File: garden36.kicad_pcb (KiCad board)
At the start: 2 copper layers, 112.1 x 90.7 mm, 41 parts, among them J1 Conn_01x02, SW1 SW_SPDT, SW2 SW_Push, U1 nice_nano

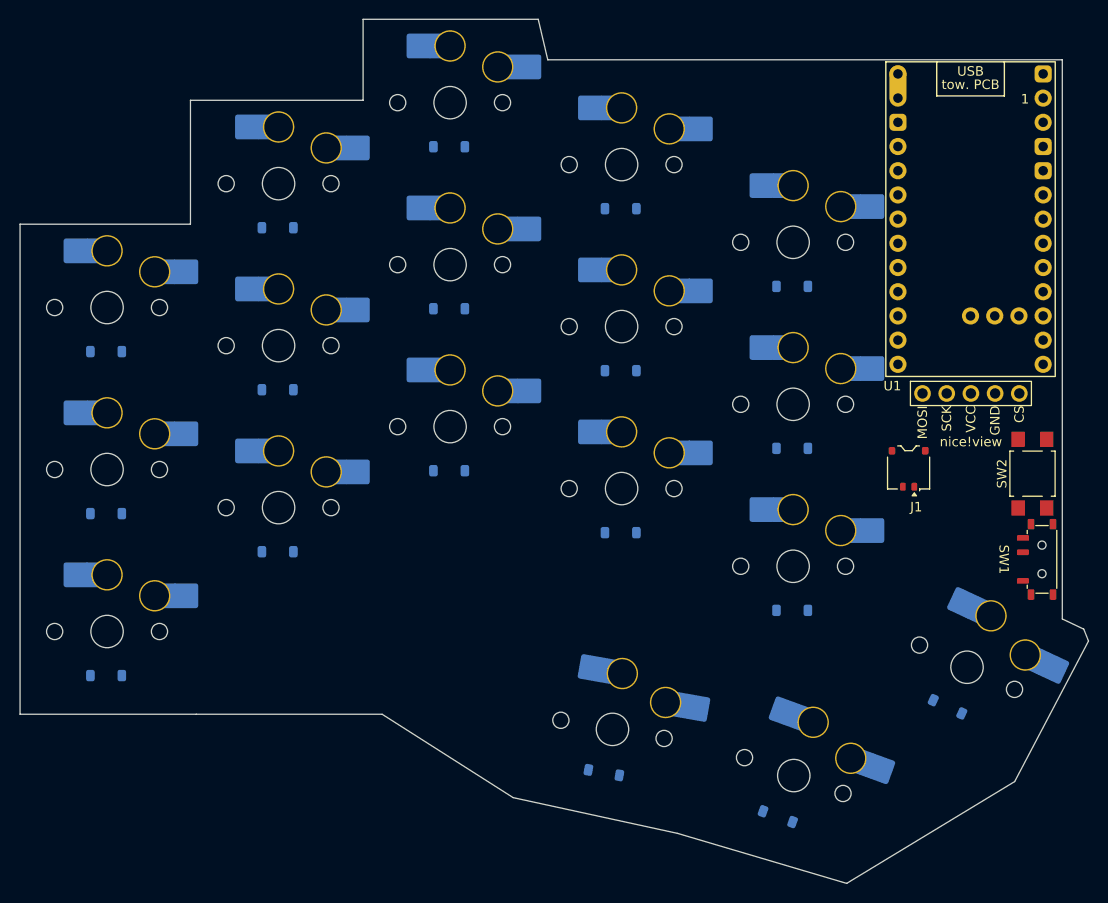
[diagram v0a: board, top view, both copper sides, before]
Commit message: Finished trace routing for left part
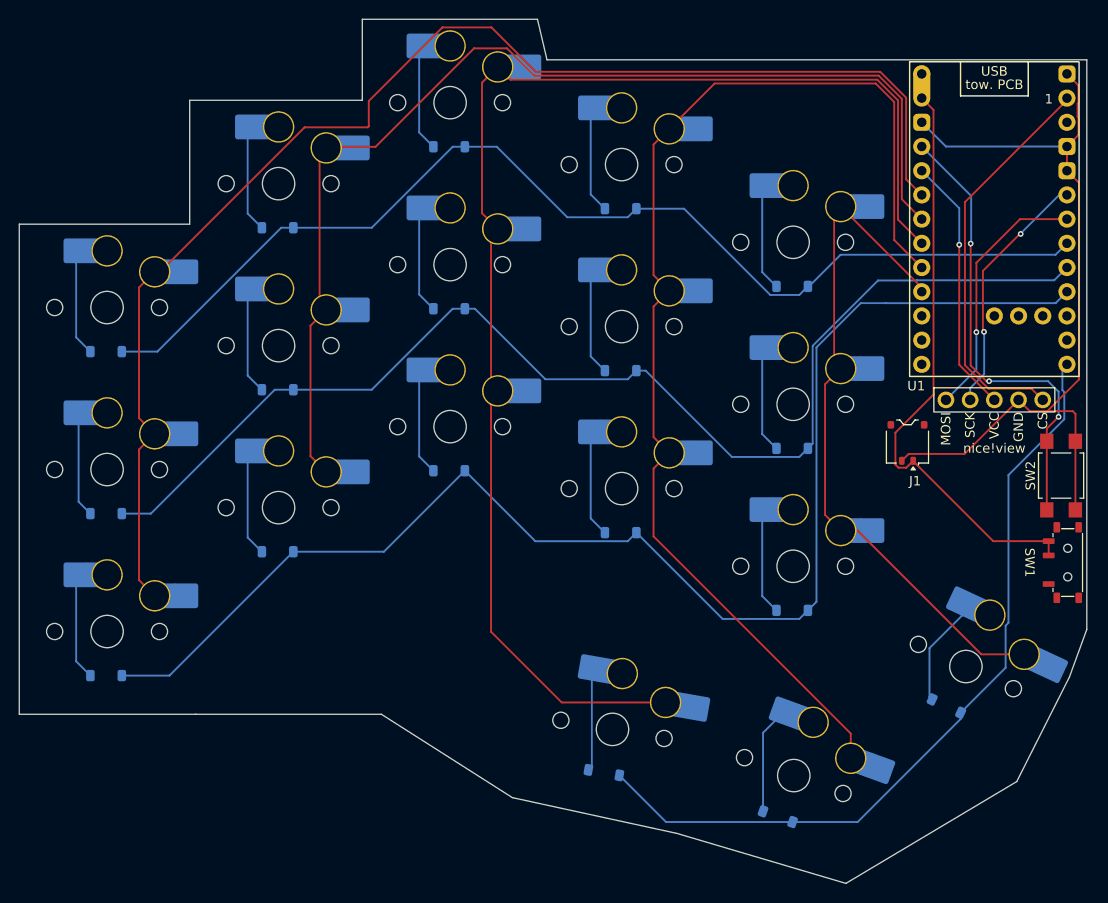
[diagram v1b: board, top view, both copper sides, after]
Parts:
- moved SW2 3.01 mm to (140.4, 96.6)
- moved J1 2.73 mm to (124.3, 93.2)
- moved SW1 2.72 mm to (141.1, 105.8)
- moved Display1 2.55 mm to (133.4, 72.2)
- moved U1 2.50 mm to (133.4, 71.0)
- moved CH18 0.14 mm to (130.4, 116.7)
- moved D18 0.14 mm to (128.4, 120.8)
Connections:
- U1 pad 10: ROW3 -> unconnected-(U1-P0.11-Pad10)
- U1 pad 12: unconnected-(U1-P1.06-LF-Pad12) -> ROW3
- U1 pad 17: unconnected-(U1-P0.31-LF-Pad17) -> COL0
- U1 pad 18: COL0 -> COL1
- U1 pad 19: COL1 -> COL2
- U1 pad 20: COL2 -> COL3
- U1 pad 21: COL3 -> COL4
- U1 pad 22: COL4 -> unconnected-(U1-P1.11-LF-Pad22)
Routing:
- net ROW2: track 0.00 -> 145.1 mm
- net COL2: track 0.00 -> 144.1 mm
- net COL0: track 0.00 -> 142.3 mm
- net ROW1: track 0.00 -> 129.5 mm
- net COL3: track 0.00 -> 123.7 mm
- net ROW0: track 0.00 -> 117.5 mm
- net COL1: track 0.00 -> 117.4 mm
- net GND: track 0.00 -> 86.2 mm
- net ROW3: track 0.00 -> 84.3 mm
- net COL4: track 0.00 -> 73.0 mm
- net BAT: track 0.00 -> 62.2 mm
- net RST: track 0.00 -> 48.4 mm, vias 0 -> 3
- net CS: track 0.00 -> 42.3 mm
- net +3.3V: track 0.00 -> 27.2 mm, vias 0 -> 1
- net MOSI: track 0.00 -> 27.1 mm, vias 0 -> 1
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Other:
- board size 112.1 x 90.7 mm -> 112 x 90.7 mm

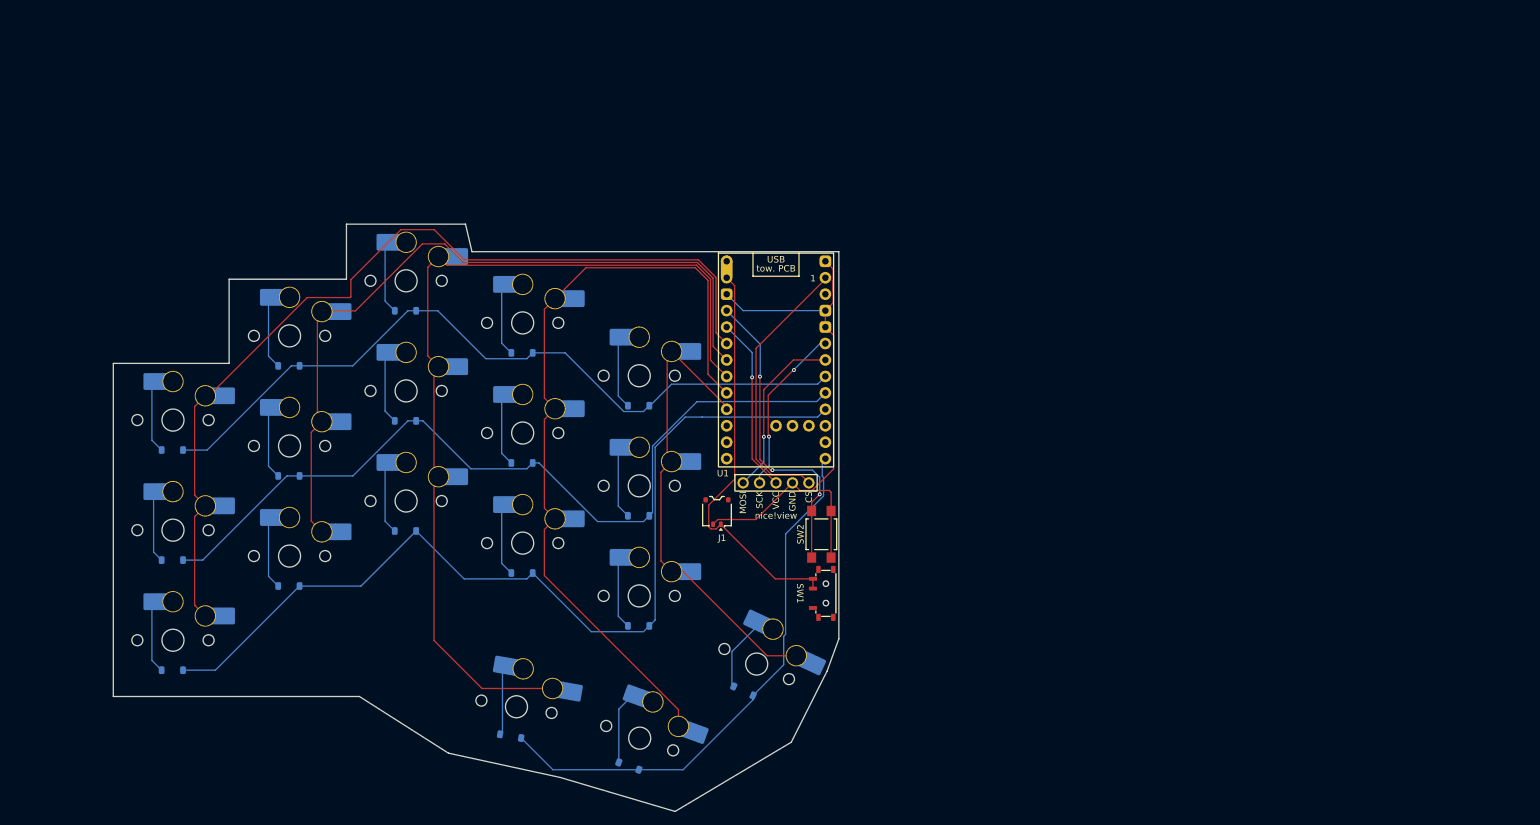
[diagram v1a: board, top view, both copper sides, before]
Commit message: Add right half of keyboard
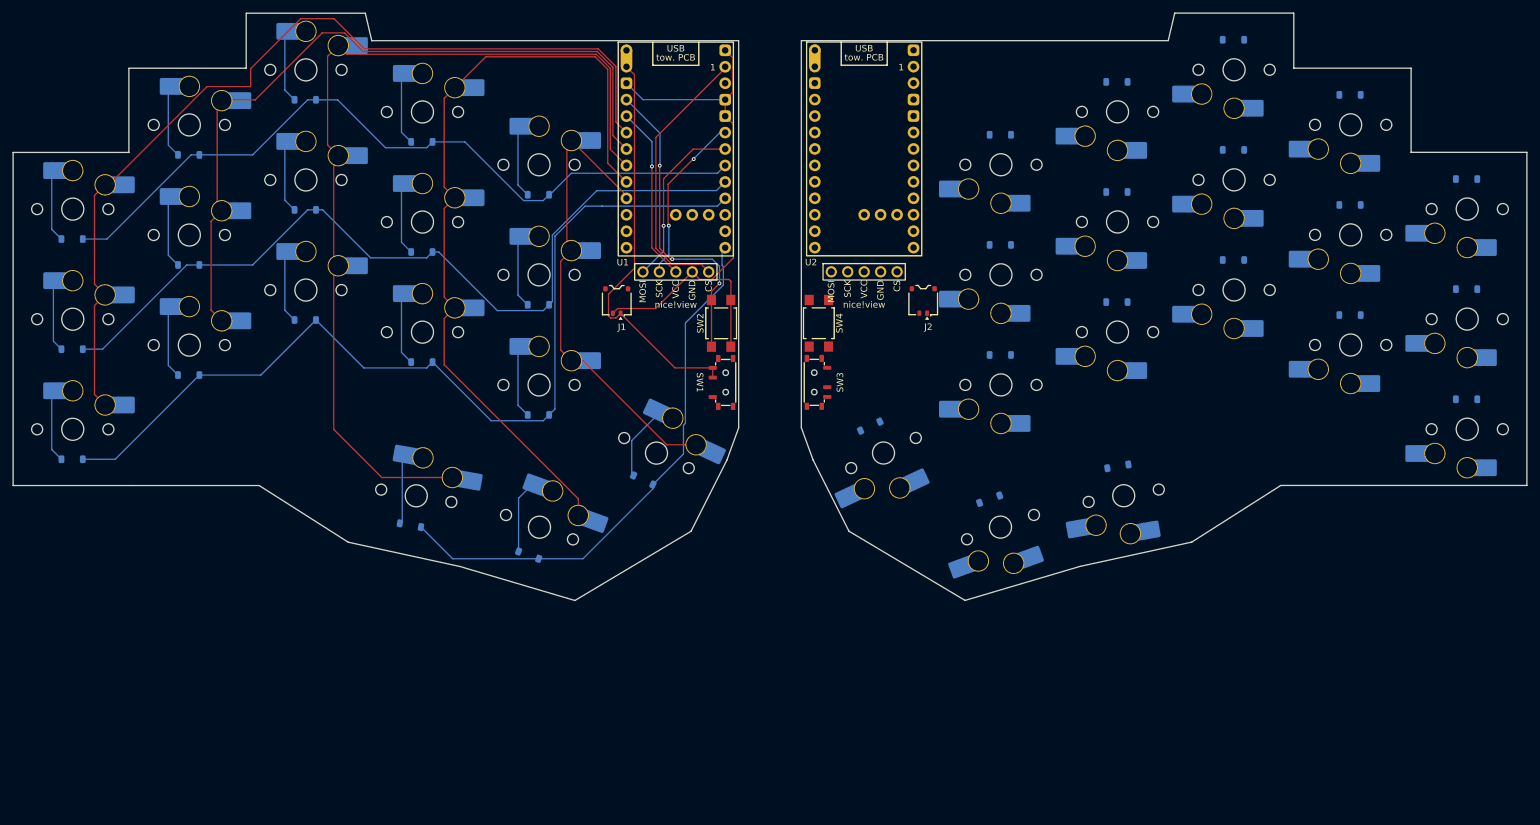
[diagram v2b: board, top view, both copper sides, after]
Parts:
- added CH19: choc_v1_SW_HS, PCM_marbastlib-choc:SW_choc_v1_HS_CPG135001S30_1u, B.Cu at (240.1, 46.4)
- added CH20: choc_v1_SW_HS, PCM_marbastlib-choc:SW_choc_v1_HS_CPG135001S30_1u, B.Cu at (222.1, 33.4)
- added CH21: choc_v1_SW_HS, PCM_marbastlib-choc:SW_choc_v1_HS_CPG135001S30_1u, B.Cu at (204.1, 24.9)
- added CH22: choc_v1_SW_HS, PCM_marbastlib-choc:SW_choc_v1_HS_CPG135001S30_1u, B.Cu at (186.1, 31.4)
- added CH23: choc_v1_SW_HS, PCM_marbastlib-choc:SW_choc_v1_HS_CPG135001S30_1u, B.Cu at (168.1, 39.6)
- added CH24: choc_v1_SW_HS, PCM_marbastlib-choc:SW_choc_v1_HS_CPG135001S30_1u, B.Cu at (240.1, 63.4)
- added CH25: choc_v1_SW_HS, PCM_marbastlib-choc:SW_choc_v1_HS_CPG135001S30_1u, B.Cu at (222.1, 50.4)
- added CH26: choc_v1_SW_HS, PCM_marbastlib-choc:SW_choc_v1_HS_CPG135001S30_1u, B.Cu at (204.1, 41.9)
- added CH27: choc_v1_SW_HS, PCM_marbastlib-choc:SW_choc_v1_HS_CPG135001S30_1u, B.Cu at (186.1, 48.4)
- added CH28: choc_v1_SW_HS, PCM_marbastlib-choc:SW_choc_v1_HS_CPG135001S30_1u, B.Cu at (168.1, 56.6)
- added CH29: choc_v1_SW_HS, PCM_marbastlib-choc:SW_choc_v1_HS_CPG135001S30_1u, B.Cu at (240.1, 80.4)
- added CH30: choc_v1_SW_HS, PCM_marbastlib-choc:SW_choc_v1_HS_CPG135001S30_1u, B.Cu at (222.1, 67.4)
- added CH31: choc_v1_SW_HS, PCM_marbastlib-choc:SW_choc_v1_HS_CPG135001S30_1u, B.Cu at (204.1, 58.9)
- added CH32: choc_v1_SW_HS, PCM_marbastlib-choc:SW_choc_v1_HS_CPG135001S30_1u, B.Cu at (186.1, 65.4)
- added CH33: choc_v1_SW_HS, PCM_marbastlib-choc:SW_choc_v1_HS_CPG135001S30_1u, B.Cu at (168.1, 73.6)
- added CH34: choc_v1_SW_HS, PCM_marbastlib-choc:SW_choc_v1_HS_CPG135001S30_1u, B.Cu at (187.1, 90.7)
- added CH35: choc_v1_SW_HS, PCM_marbastlib-choc:SW_choc_v1_HS_CPG135001S30_1u, B.Cu at (168.0, 95.5)
- added CH36: choc_v1_SW_HS, PCM_marbastlib-choc:SW_choc_v1_HS_CPG135001S30_1u, B.Cu at (150.0, 84.1)
- added D19: 1N4148W, Diode_SMD:D_SOD-123, B.Cu at (240.0, 41.8)
- added D20: 1N4148W, Diode_SMD:D_SOD-123, B.Cu at (222.0, 28.8)
- added D21: 1N4148W, Diode_SMD:D_SOD-123, B.Cu at (204.0, 20.3)
- added D22: 1N4148W, Diode_SMD:D_SOD-123, B.Cu at (186.0, 26.8)
- added D23: 1N4148W, Diode_SMD:D_SOD-123, B.Cu at (168.0, 34.9)
- added D24: 1N4148W, Diode_SMD:D_SOD-123, B.Cu at (240.0, 58.8)
- added D25: 1N4148W, Diode_SMD:D_SOD-123, B.Cu at (222.0, 45.8)
- added D26: 1N4148W, Diode_SMD:D_SOD-123, B.Cu at (204.0, 37.3)
- added D27: 1N4148W, Diode_SMD:D_SOD-123, B.Cu at (186.0, 43.8)
- added D28: 1N4148W, Diode_SMD:D_SOD-123, B.Cu at (168.0, 51.9)
- added D29: 1N4148W, Diode_SMD:D_SOD-123, B.Cu at (240.0, 75.8)
- added D30: 1N4148W, Diode_SMD:D_SOD-123, B.Cu at (222.0, 62.8)
- added D31: 1N4148W, Diode_SMD:D_SOD-123, B.Cu at (204.0, 54.3)
- added D32: 1N4148W, Diode_SMD:D_SOD-123, B.Cu at (186.0, 60.8)
- added D33: 1N4148W, Diode_SMD:D_SOD-123, B.Cu at (168.0, 68.9)
- added D34: 1N4148W, Diode_SMD:D_SOD-123, B.Cu at (186.2, 86.1)
- added D35: 1N4148W, Diode_SMD:D_SOD-123, B.Cu at (166.4, 91.2)
- added D36: 1N4148W, Diode_SMD:D_SOD-123, B.Cu at (147.9, 79.9)
- added Display2: nice!view, nice_view:nice_view, F.Cu at (147.0, 39.6)
- added J2: Conn_01x02, PCM_marbastlib-various:CON_JST_ACH_BM02B, F.Cu at (156.1, 60.6)
- added SW3: SW_SPDT, PCM_marbastlib-various:SW_MSK12C02-HB, F.Cu at (139.3, 73.2)
- added SW4: SW_Push, Button_Switch_SMD:SW_SPST_TL3305A, F.Cu at (140.0, 64.0)
- added U2: nice_nano, PCM_marbastlib-xp-promicroish:nice_nano_AH_USBdn, F.Cu at (147.0, 38.4)
- moved CH10 36.1 mm to (96.8, 56.6)
- moved CH13 36.1 mm to (60.8, 58.9)
- moved CH5 36.1 mm to (96.8, 39.6)
- moved CH8 36.1 mm to (60.8, 41.9)
- moved CH9 36.1 mm to (78.8, 48.4)
- moved D1 36.1 mm to (24.7, 51.0)
- moved D10 36.1 mm to (96.7, 61.2)
- moved D2 36.1 mm to (42.7, 38.0)
- moved D4 36.1 mm to (78.7, 36.0)
- moved D5 36.1 mm to (96.7, 44.2)
- moved D7 36.1 mm to (42.7, 55.0)
- moved D9 36.1 mm to (78.7, 53.0)
- moved J1 36.1 mm to (108.8, 60.6)
- moved U1 36.1 mm to (117.9, 38.4)
- moved CH1 36.1 mm to (24.8, 46.4)
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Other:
- board size 112 x 90.7 mm -> 233.7 x 90.7 mm

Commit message: Finished routing for both halfs
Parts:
- moved CH29 72.9 mm to (186.1, 31.4)
- moved D29 72.9 mm to (186.0, 26.8)
- moved CH21 66.2 mm to (240.1, 80.4)
- moved D21 66.2 mm to (240.0, 75.8)
- moved CH23 55.1 mm to (222.1, 50.4)
- moved D23 55.1 mm to (222.0, 45.8)
- moved CH30 40.7 mm to (186.1, 48.4)
- moved D30 40.7 mm to (186.0, 43.8)
- moved CH34 39.0 mm to (168.1, 56.6), turned to 180 degrees
- moved CH28 39.0 mm to (187.1, 90.7), turned to -170 degrees
- moved D28 38.7 mm to (186.2, 86.1), turned to 10 degrees
- moved D34 38.7 mm to (168.0, 51.9), turned to 0 degrees
- moved D32 36.2 mm to (166.4, 91.2), turned to 20 degrees
- moved CH22 36.1 mm to (222.1, 33.4)
- moved D22 36.1 mm to (222.0, 28.8)
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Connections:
- U2 pad 10: unconnected-(U2-P0.11-Pad10) -> COL8
- U2 pad 11: unconnected-(U2-P1.04-LF-Pad11) -> COL9
- U2 pad 12: ROW7 -> unconnected-(U2-P1.06-LF-Pad12)
- U2 pad 17: COL5 -> unconnected-(U2-P0.31-LF-Pad17)
- U2 pad 18: COL6 -> unconnected-(U2-P0.29-LF-Pad18)
- U2 pad 19: COL7 -> unconnected-(U2-P0.02-LF-Pad19)
- U2 pad 20: COL8 -> unconnected-(U2-P1.15-LF-Pad20)
- U2 pad 21: COL9 -> ROW4
- U2 pad 22: unconnected-(U2-P1.11-LF-Pad22) -> ROW5
- U2 pad 23: unconnected-(U2-P0.10-LF-Pad23) -> ROW6
- U2 pad 24: unconnected-(U2-P0.09-LF-Pad24) -> ROW7
- U2 pad 7: ROW4 -> COL5
- U2 pad 8: ROW5 -> COL6
- U2 pad 9: ROW6 -> COL7
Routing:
- net COL5: track 0.00 -> 147.3 mm
- net COL7: track 0.00 -> 142.2 mm
- net ROW6: track 0.00 -> 135.1 mm
- net COL8: track 0.00 -> 129.9 mm
- net COL6: track 0.00 -> 123.8 mm
- net ROW4: track 0.00 -> 122.9 mm
- net ROW5: track 0.00 -> 118.9 mm
- net GNDx: track 0.00 -> 91.4 mm
- net ROW7: track 0.00 -> 79.7 mm
- net BATx: track 0.00 -> 72.6 mm
- net COL9: track 0.00 -> 69.1 mm
- net RSTx: track 0.00 -> 40.1 mm, vias 0 -> 1
- net CSx: track 0.00 -> 33.4 mm
- net SCKx: track 0.00 -> 29.9 mm, vias 0 -> 1
- net MOSIx: track 0.00 -> 29.4 mm, vias 0 -> 1
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
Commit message: Filled zones for both halfs
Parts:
- moved D19 40.7 mm to (260.3, 77.1)
- moved D20 40.7 mm to (260.3, 94.1)
- moved D21 40.7 mm to (260.3, 111.1)
- moved CH33 40.7 mm to (188.4, 74.9)
- moved CH34 40.7 mm to (188.4, 91.9)
- moved D23 40.7 mm to (242.3, 81.1)
- moved D26 40.7 mm to (224.3, 72.6)
- moved D27 40.7 mm to (224.3, 89.6)
- moved D28 40.7 mm to (206.5, 121.4)
- moved D33 40.7 mm to (188.3, 70.2)
- moved D34 40.7 mm to (188.3, 87.2)
- moved D35 40.7 mm to (188.3, 104.2)
- moved Display2 40.7 mm to (167.3, 74.9)
- moved CH29 40.7 mm to (206.4, 66.7)
- moved CH30 40.7 mm to (206.4, 83.7)
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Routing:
- added copper zone on B.Cu, net (none)
- added copper zone on F.Cu, net (none)
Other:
- board size 233.7 x 90.7 mm -> 246.1 x 91.1 mm

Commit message: V1 ordered
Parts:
- added REF**: MountingHole_2.2mm_M2, MountingHole:MountingHole_2.2mm_M2, F.Cu at (237.4, 71.1)
- added REF**: MountingHole_2.2mm_M2, MountingHole:MountingHole_2.2mm_M2, F.Cu at (111.7, 64.3)
- added REF**: MountingHole_2.2mm_M2, MountingHole:MountingHole_2.2mm_M2, F.Cu at (46.7, 124.6)
- added REF**: mousebites 1mm, PCM_marbastlib-various:mousebites_1mm, B.Cu at (135.8, 99.3)
- added REF**: MountingHole_2.2mm_M2, MountingHole:MountingHole_2.2mm_M2, F.Cu at (121.9, 106.6)
- added REF**: MountingHole_2.2mm_M2, MountingHole:MountingHole_2.2mm_M2, F.Cu at (154.6, 106.6)
- added REF**: mousebites 1mm, PCM_marbastlib-various:mousebites_1mm, F.Cu at (140.8, 99.3)
- added REF**: MountingHole_2.2mm_M2, MountingHole:MountingHole_2.2mm_M2, F.Cu at (39.2, 71.1)
- added REF**: MountingHole_2.2mm_M2, MountingHole:MountingHole_2.2mm_M2, F.Cu at (164.9, 64.3)
- added REF**: MountingHole_2.2mm_M2, MountingHole:MountingHole_2.2mm_M2, F.Cu at (119.9, 133.8)
- added REF**: MountingHole_2.2mm_M2, MountingHole:MountingHole_2.2mm_M2, F.Cu at (156.7, 133.8)
- added REF**: MountingHole_2.2mm_M2, MountingHole:MountingHole_2.2mm_M2, F.Cu at (229.9, 124.6)
- added by shnaps: LOGO, LOGO, F.Cu at (209.6, 119.3)
- added garden36: LOGO, LOGO, F.Cu at (63.1, 119.3)
- J1, J2: footprint PCM_marbastlib-various:CON_JST_ACH_BM02B -> Connector_JST:JST_PH_S2B-PH-K_1x02_P2.00mm_Horizontal
- moved D19 16.6 mm to (243.8, 77.5)
- moved D20 16.6 mm to (243.8, 94.5)
- moved D21 16.6 mm to (243.8, 111.5)
- moved D36 16.6 mm to (151.7, 115.6)
- moved CH19 16.6 mm to (243.9, 82.1)
- moved CH20 16.6 mm to (243.9, 99.1)
- moved CH21 16.6 mm to (243.9, 116.1)
- moved CH22 16.6 mm to (225.9, 69.1)
- moved CH23 16.6 mm to (225.9, 86.1)
- moved CH24 16.6 mm to (225.9, 103.1)
- moved CH25 16.6 mm to (207.9, 60.6)
- moved CH26 16.6 mm to (207.9, 77.6)
- moved CH27 16.6 mm to (207.9, 94.6)
- moved CH28 16.6 mm to (190.8, 126.4)
- moved CH29 16.6 mm to (189.9, 67.1)
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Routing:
- net GNDx: track 91.4 -> 101.9 mm
- net BATx: track 72.6 -> 78.6 mm
- net BAT: track 62.2 -> 67.3 mm
- net RSTx: track 40.1 -> 44.0 mm
- net RST: track 48.4 -> 51.8 mm
- net GND: track 86.1 -> 89.5 mm
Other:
- board size 246.1 x 91.1 mm -> 231.5 x 91.8 mm
- board text added: "v1.0"
